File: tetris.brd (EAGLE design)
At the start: 100 x 80 mm, 19 parts, among them IC1 78L24Z, U1 328P, Y1 16MHz

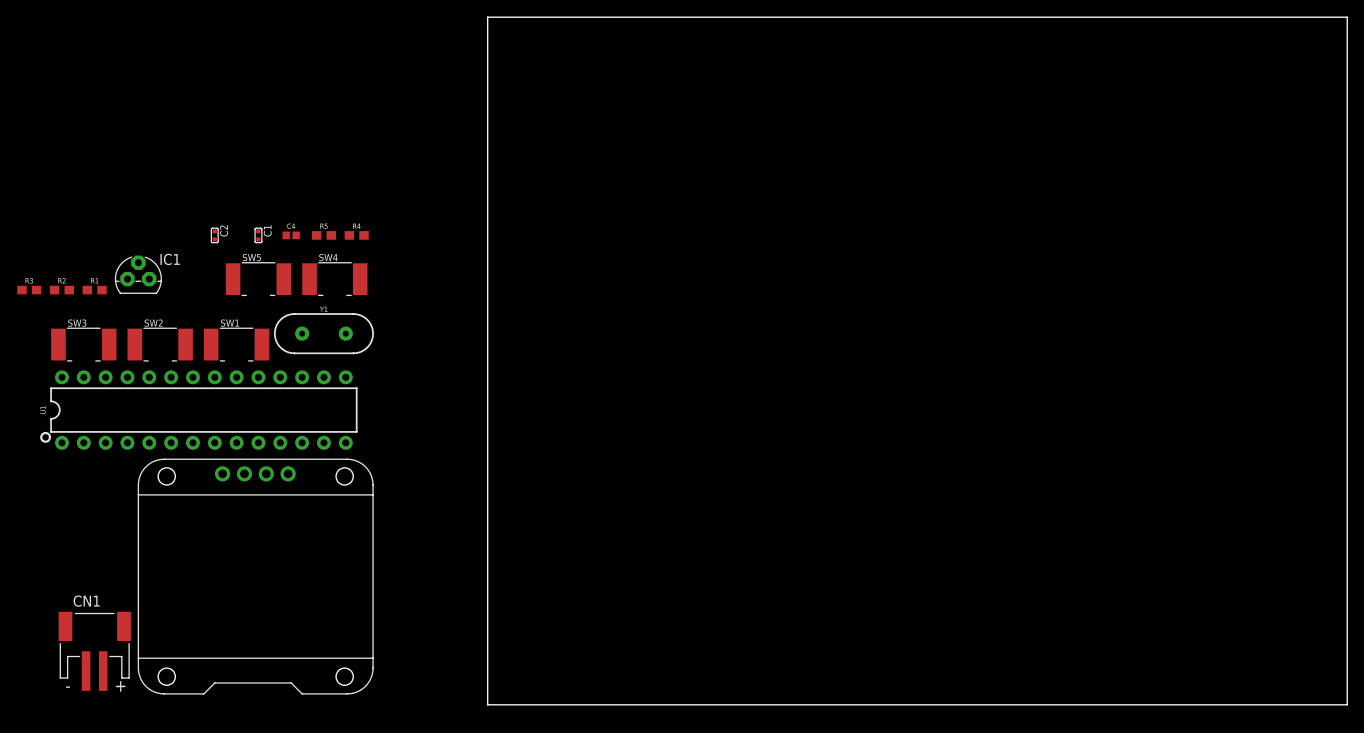
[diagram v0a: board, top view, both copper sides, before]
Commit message: Added gitignore and autoroute
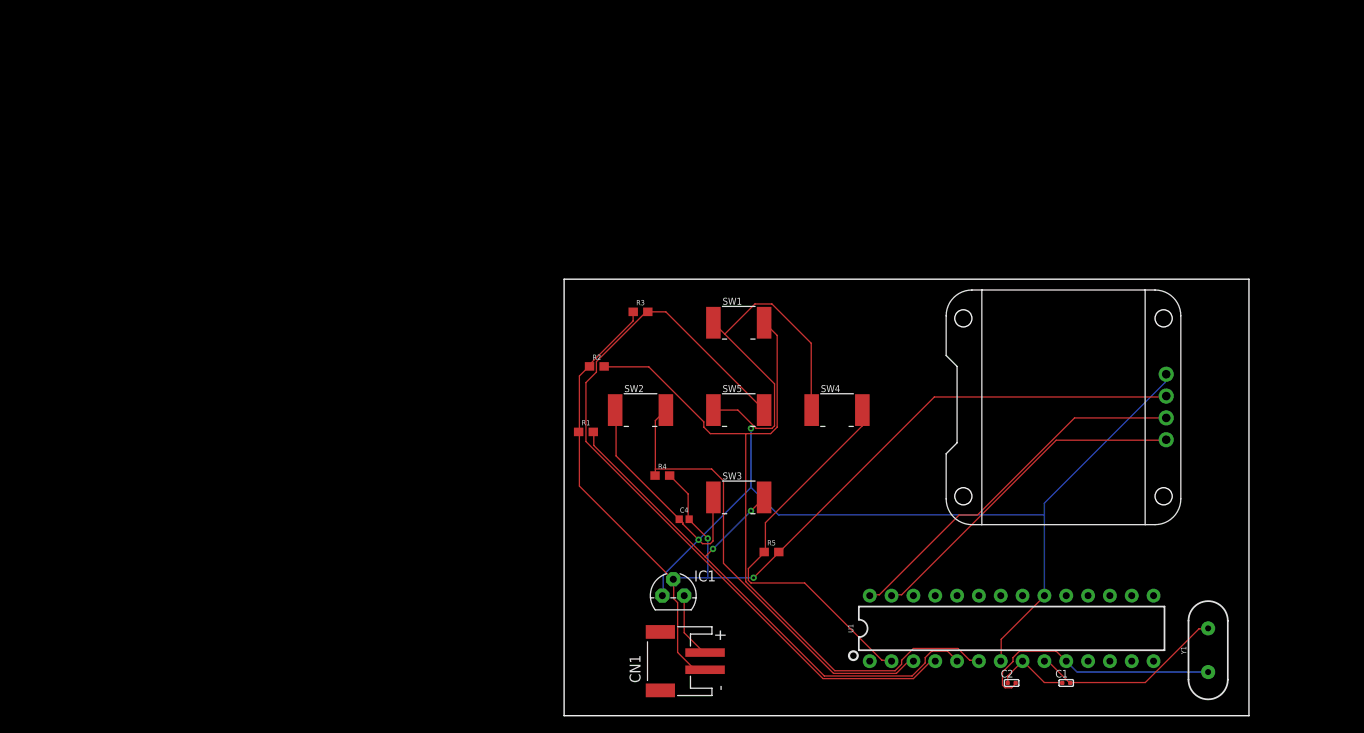
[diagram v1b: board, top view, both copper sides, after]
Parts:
- moved Y1 109.3 mm to (83.8, 6.35), turned to 90 degrees
- moved C1 107.4 mm to (67.3, 2.54), turned to 90 degrees
- moved C2 106.3 mm to (61.0, 2.54), turned to 90 degrees
- moved U1 97.4 mm to (61.0, 8.89)
- moved U$1 95.9 mm to (67.3, 34.3), turned to 270 degrees
- moved SW3 78.2 mm to (29.2, 24.1)
- moved IC1 72.3 mm to (21.6, 12.7)
- moved R3 71.2 mm to (17.8, 45.7)
- moved CN1 67.4 mm to (21.6, 5.08), turned to 90 degrees
- moved R5 63.8 mm to (33.0, 17.8)
- moved R2 62.9 mm to (12.7, 39.4)
- moved SW4 60.4 mm to (40.6, 34.3)
- moved R1 59.5 mm to (11.4, 31.8)
- moved SW1 58.5 mm to (29.2, 44.5)
- moved SW5 57.9 mm to (29.2, 34.3)
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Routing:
- net VCC: track 0.00 -> 171.6 mm, vias 0 -> 2
- net GND: track 0.00 -> 131.2 mm, vias 0 -> 2
- net N$3: track 0.00 -> 89.3 mm
- net N$1: track 0.00 -> 87.5 mm
- net N$2: track 0.00 -> 66.8 mm, vias 0 -> 2
- net N$4: track 0.00 -> 54.3 mm
- net N$5: track 0.00 -> 45.9 mm
- net N$11: track 0.00 -> 43.1 mm
- net N$10: track 0.00 -> 39.5 mm
- net N$7: track 0.00 -> 29.7 mm
- net N$6: track 0.00 -> 22.8 mm
- net N$8: track 0.00 -> 8.91 mm
- net N$13: track 0.00 -> 7.70 mm
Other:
- board size 100 x 80 mm -> 79.7 x 50.8 mm

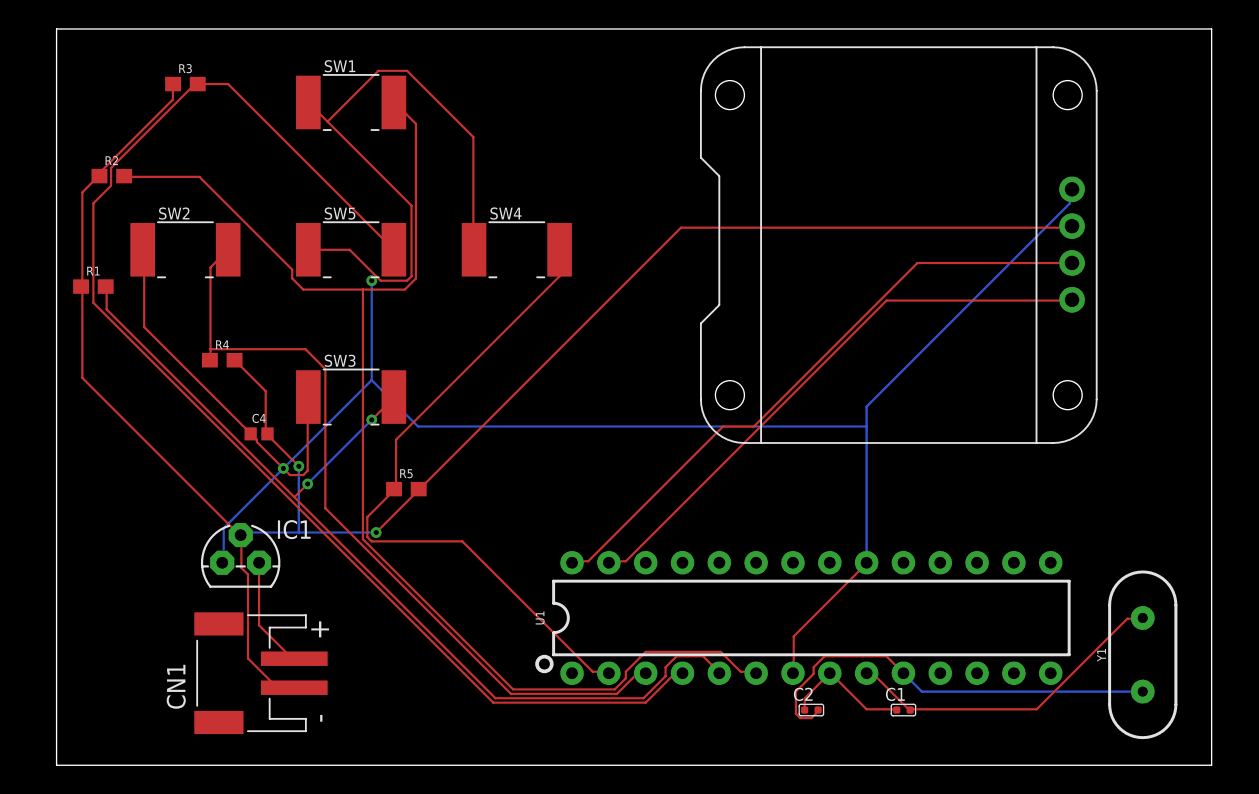
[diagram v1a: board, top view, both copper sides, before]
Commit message: added an on off switch
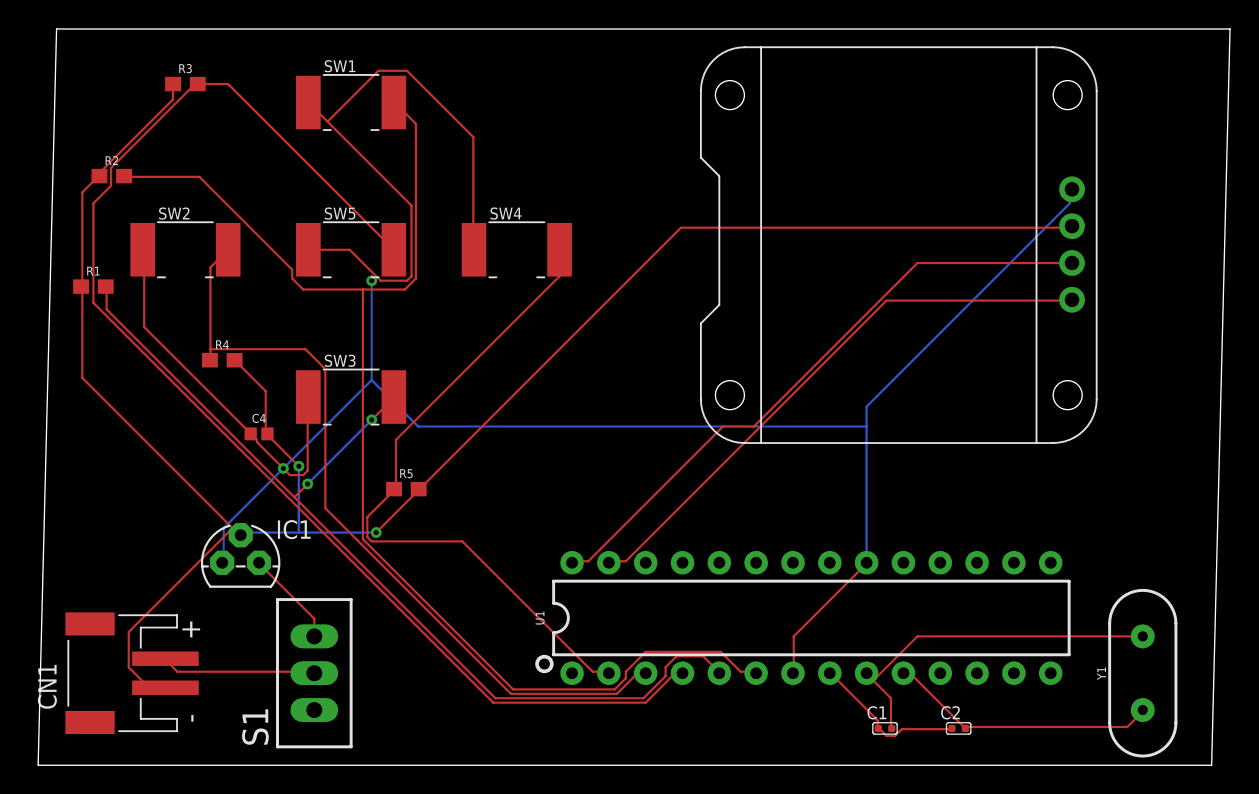
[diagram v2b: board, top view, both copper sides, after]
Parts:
- added S1: TL38PO, switch:TL3XPO
- moved C2 10.2 mm to (71.1, 1.27)
- moved CN1 8.89 mm to (12.7, 5.08)
- moved C1 1.80 mm to (66.0, 1.27)
- moved Y1 1.27 mm to (83.8, 5.08)
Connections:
- removed net N$13: CN1.1, IC1.3
- new net N$12: IC1.3, S1.3
- new net N$9: CN1.1, S1.2
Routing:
- net N$7: track 29.7 -> 18.7 mm
- net N$9: track 0.00 -> 10.8 mm
- net N$13: track 7.70 -> 0.00 mm
- net N$12: track 0.00 -> 6.66 mm
- net GND: track 131.2 -> 134.8 mm
- net N$6: track 22.8 -> 25.1 mm
- net N$8: track 8.91 -> 10.7 mm
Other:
- board size 79.7 x 50.8 mm -> 82.2 x 50.8 mm
